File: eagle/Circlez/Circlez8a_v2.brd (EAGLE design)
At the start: 50 x 50 mm, 55 parts, among them IC1 MEGA8-AI, J1 AVR_SPI_PRG_6PTH

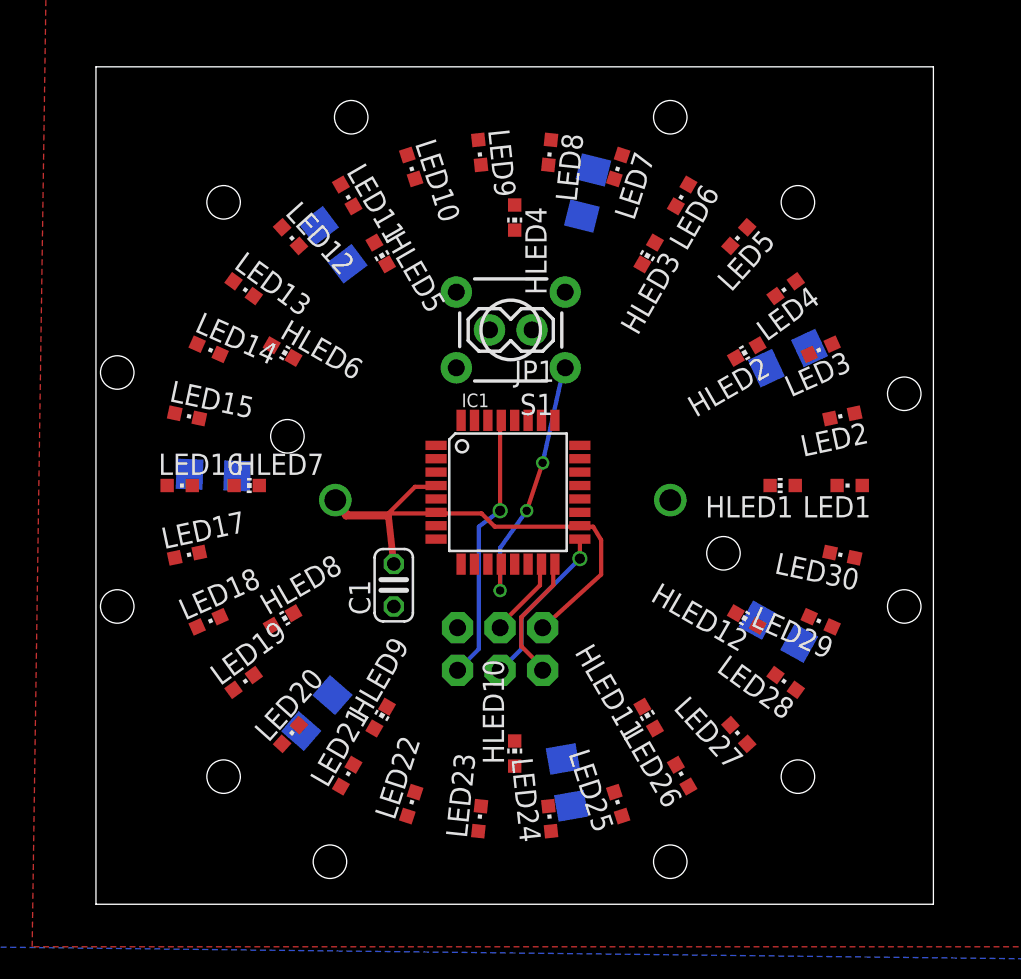
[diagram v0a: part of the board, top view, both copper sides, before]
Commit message: Wiring and placement ok. TODO double check and add labels. Add a SMD rtc on the back ?
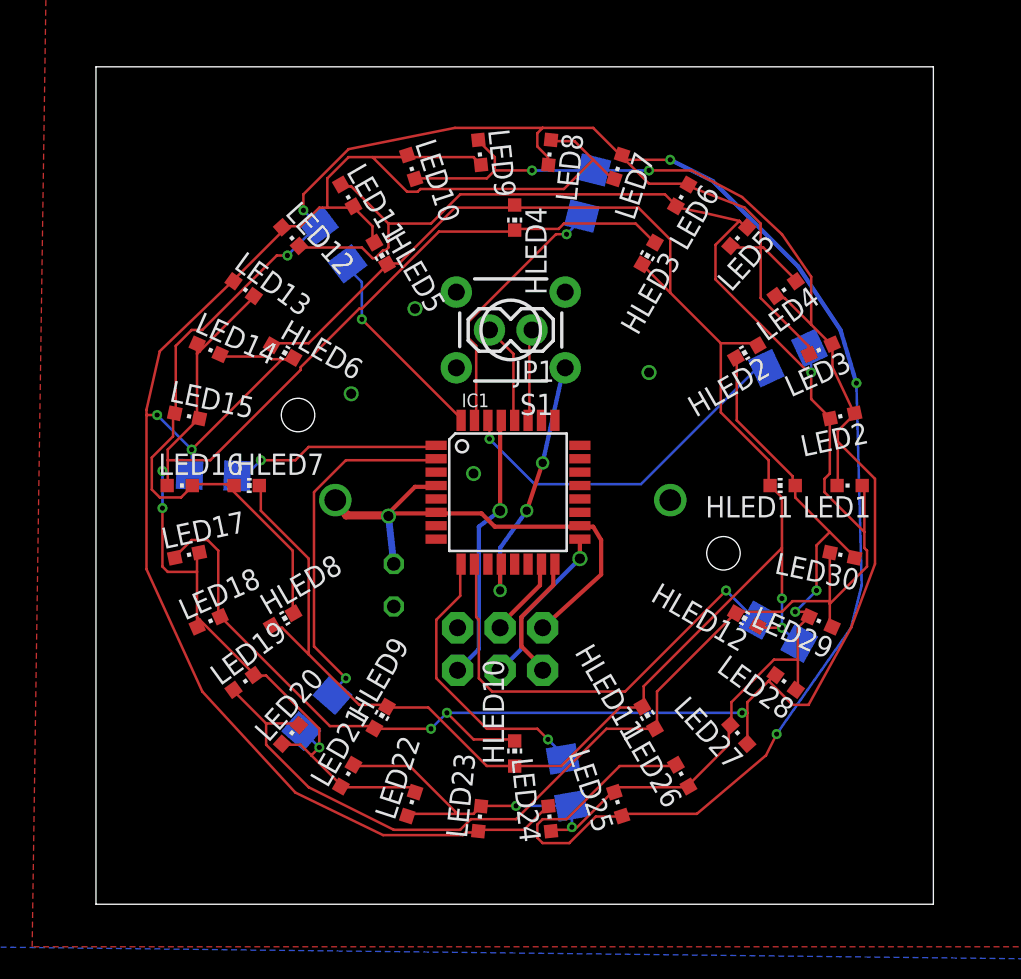
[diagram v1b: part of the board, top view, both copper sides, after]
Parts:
- flipped C1 to the bottom
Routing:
- net N$9: track 0.00 -> 156.1 mm, vias 0 -> 5
- net N$2: track 0.00 -> 119.6 mm, vias 0 -> 1
- net N$8: track 0.00 -> 117.4 mm, vias 0 -> 5
- net N$14: track 0.00 -> 113.0 mm, vias 0 -> 2
- net N$10: track 0.00 -> 112.6 mm, vias 0 -> 2
- net N$11: track 0.00 -> 85.0 mm, vias 0 -> 3
- net N$13: track 0.00 -> 65.6 mm, vias 0 -> 4
- net N$21: track 0.00 -> 27.1 mm, vias 0 -> 1
- net N$15: track 0.00 -> 21.8 mm, vias 0 -> 1
- net N$19: track 0.00 -> 21.5 mm, vias 0 -> 1
- net N$20: track 0.00 -> 17.1 mm, vias 0 -> 1
- net N$16: track 0.00 -> 15.6 mm, vias 0 -> 1
- net N$18: track 0.00 -> 12.6 mm, vias 0 -> 1
- net N$17: track 0.00 -> 12.2 mm, vias 0 -> 1
- net N$12: track 0.00 -> 6.01 mm
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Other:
- board text removed: "1"
- board text removed: "2"
- board text removed: "24"

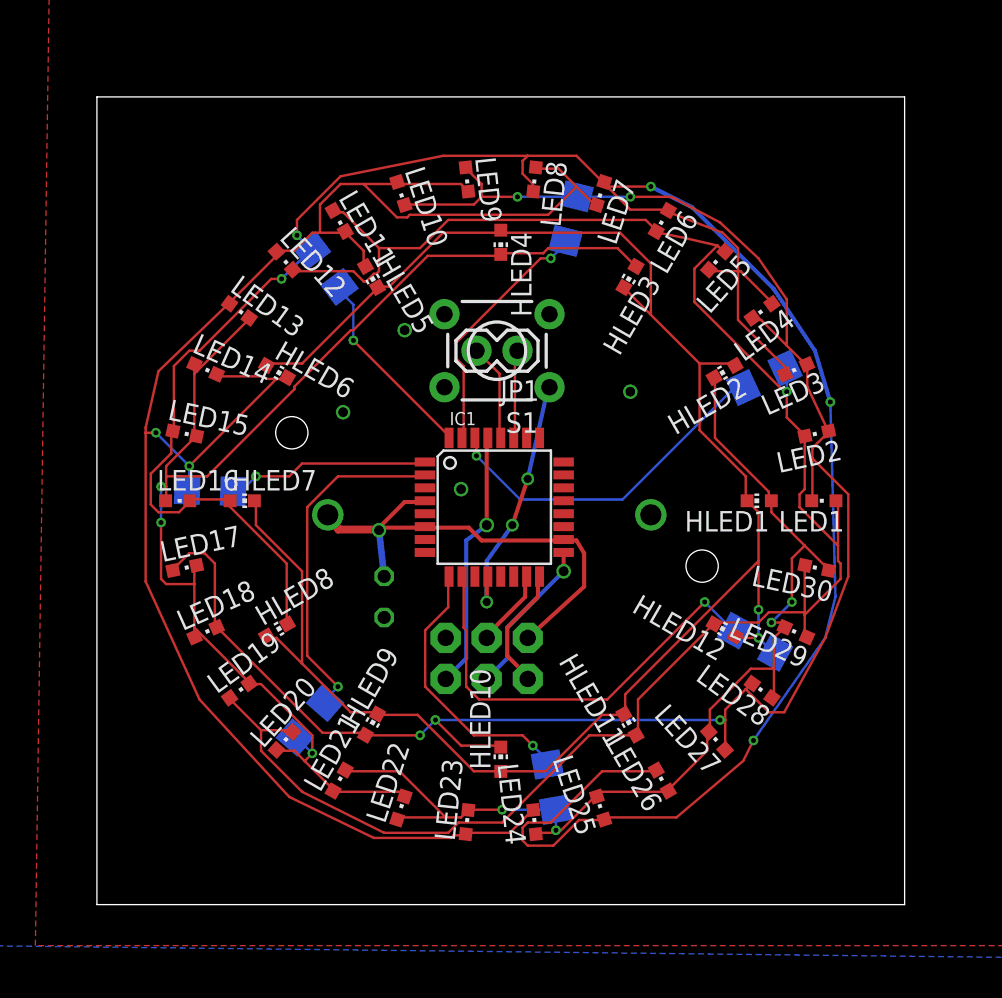
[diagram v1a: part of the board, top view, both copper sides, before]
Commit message: Made board circular
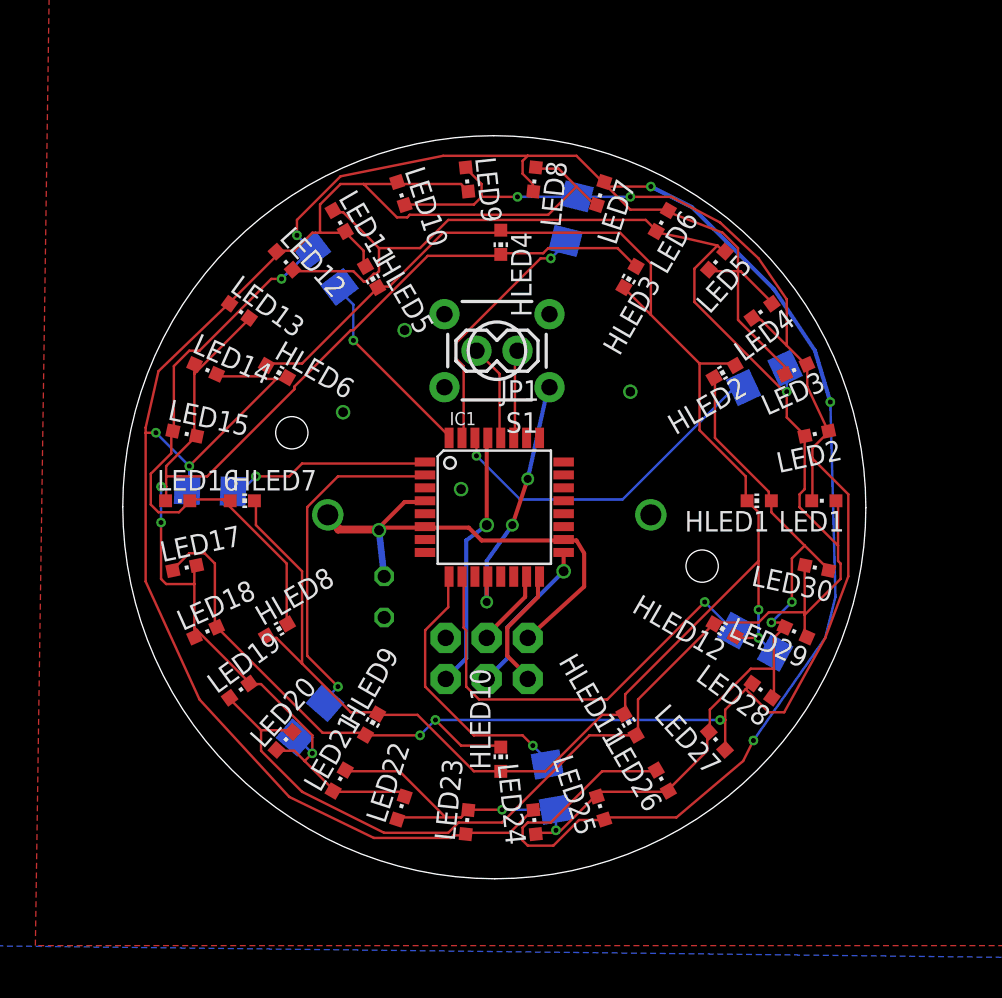
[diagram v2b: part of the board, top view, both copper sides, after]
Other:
- board size 50 x 50 mm -> 46 x 46 mm
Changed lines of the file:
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@@
 <board>
 <plain>
-<wire x1="0" y1="0" x2="50" y2="0" width="0" layer="20"/>
-<wire x1="50" y1="0" x2="50" y2="50" width="0" layer="20"/>
-<wire x1="50" y1="50" x2="0" y2="50" width="0" layer="20"/>
-<wire x1="0" y1="50" x2="0" y2="0" width="0" layer="20"/>
+<wire x1="1.6" y1="24.630575" x2="24.630575" y2="1.6" width="0" layer="20" curve="90"/>
+<wire x1="24.630575" y1="1.6" x2="47.6" y2="24.569425" width="0" layer="20" curve="90"/>
+<wire x1="47.6" y1="24.569425" x2="24.569425" y2="47.6" width="0" layer="20" curve="90"/>
+<wire x1="24.569425" y1="47.6" x2="1.6" y2="24.630575" width="0" layer="20" curve="90"/>
 <circle x="24.6" y="24.6" radius="23" width="0.4064" layer="48"/>
 <text x="21.59" y="21.59" size="0.8128" layer="48" font="vector">ATmega8a</text>
@@
 <rectangle x1="25.4" y1="12.065" x2="27.94" y2="15.24" layer="52"/>
 <text x="44.45" y="26.035" size="1.27" layer="52" font="vector" rot="MR0">http://kalshagar.wikispaces.com/Circlez</text>
-<text x="36.83" y="29.21" size="1.4224" layer="52" font="vector" rot="MR0">Circlez - v2.0 March2014</text>
+<text x="38.1" y="29.21" size="1.4224" layer="52" font="vector" rot="MR0">Circlez - v2.0 March2014</text>
 <hole x="37.465" y="20.955" drill="2"/>
 <hole x="12.065" y="29.21" drill="2"/>

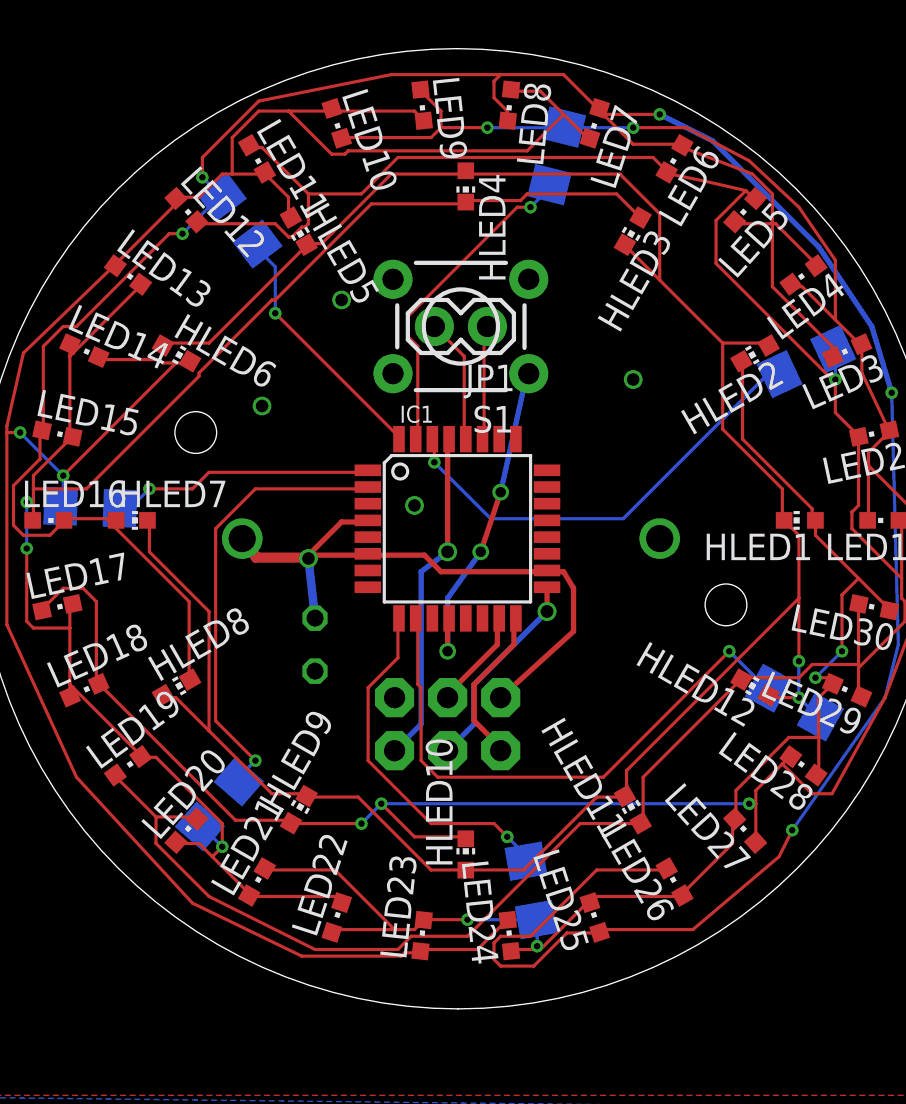
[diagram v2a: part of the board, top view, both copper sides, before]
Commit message: Added DS1307 and pads for 5v.
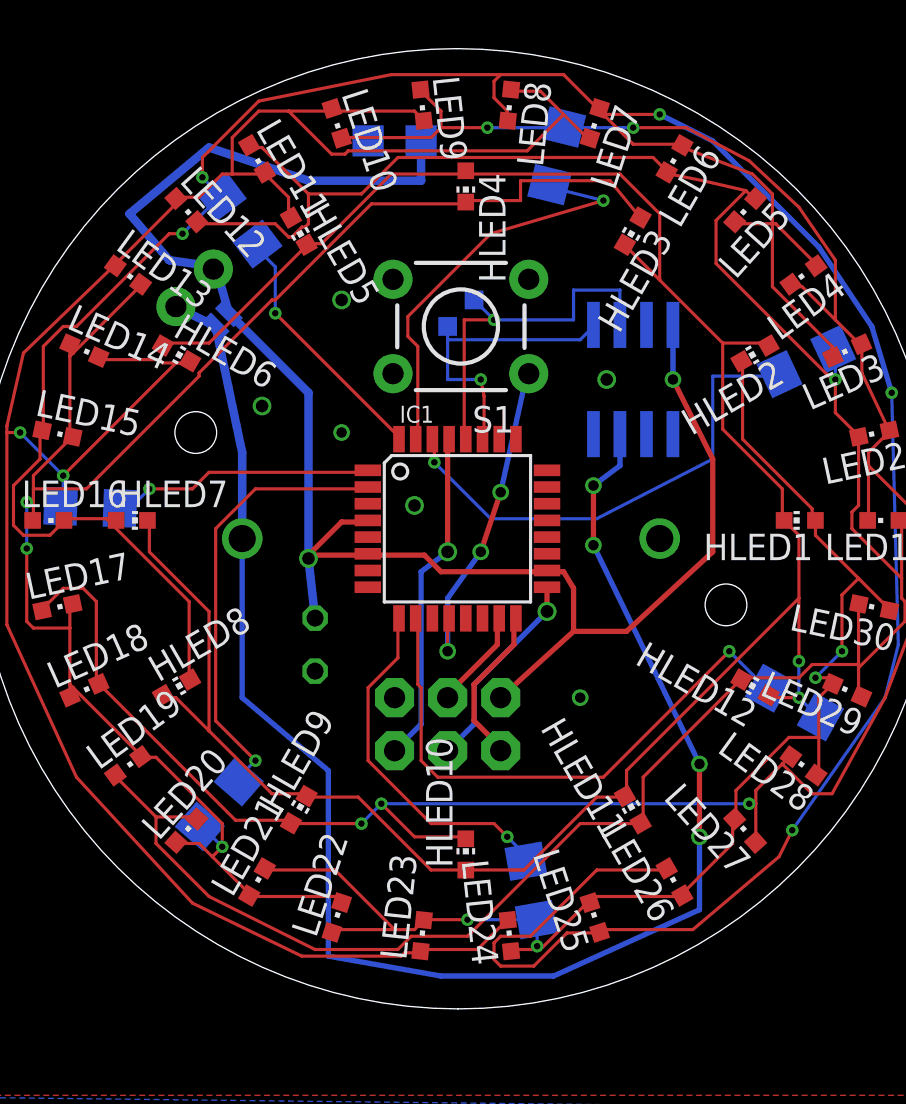
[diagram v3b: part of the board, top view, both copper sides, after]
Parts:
- removed JP1: (no value), SparkFun-Connectors:1X02
- added GND, VCC: PTR1TP15SQ, testpad:TP15SQ
- added JP2: (no value), SparkFun-Passives:SJ_2S-NO
- added JP3: (no value), SparkFun-Passives:1X02
- added TP_SCL, TP_SDA: PTR1TP09SQ, testpad:TP09SQ
- added U$2: DS1307SO8, SparkFun-FreqCtrl:SO08
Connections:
- removed net N$34: IC1.27, JP1.1
- new net N$24: IC1.27, TP_SDA.TP, U$2.5
- new net VBAT: BAT1.1, JP2.1, JP3.1, U$2.3
- net GND: now also GND.TP, U$2.4
- net N$12: now also TP_SCL.TP, U$2.6; no longer JP1.2
- net VCC: now also JP2.2, JP3.2, U$2.8, VCC.TP; no longer BAT1.1
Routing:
- net VBAT: track 0.00 -> 77.6 mm, vias 0 -> 4
- net VCC: track 34.0 -> 84.3 mm, vias 1 -> 2
- net N$24: track 0.00 -> 14.3 mm, vias 0 -> 1
- net N$12: track 6.01 -> 17.7 mm, vias 0 -> 1
- net N$34: track 5.48 -> 0.00 mm
- net N$16: track 15.6 -> 20.1 mm
- net N$15: track 21.8 -> 23.6 mm
- net N$11: track 85.0 -> 86.2 mm
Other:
- board text added: "VBAT"
- board text added: "VCC 5v"
- board text added: "VCC=VBAT"
